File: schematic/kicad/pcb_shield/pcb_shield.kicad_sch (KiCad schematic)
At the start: 15 parts, among them J1 CN7, J2 CN10

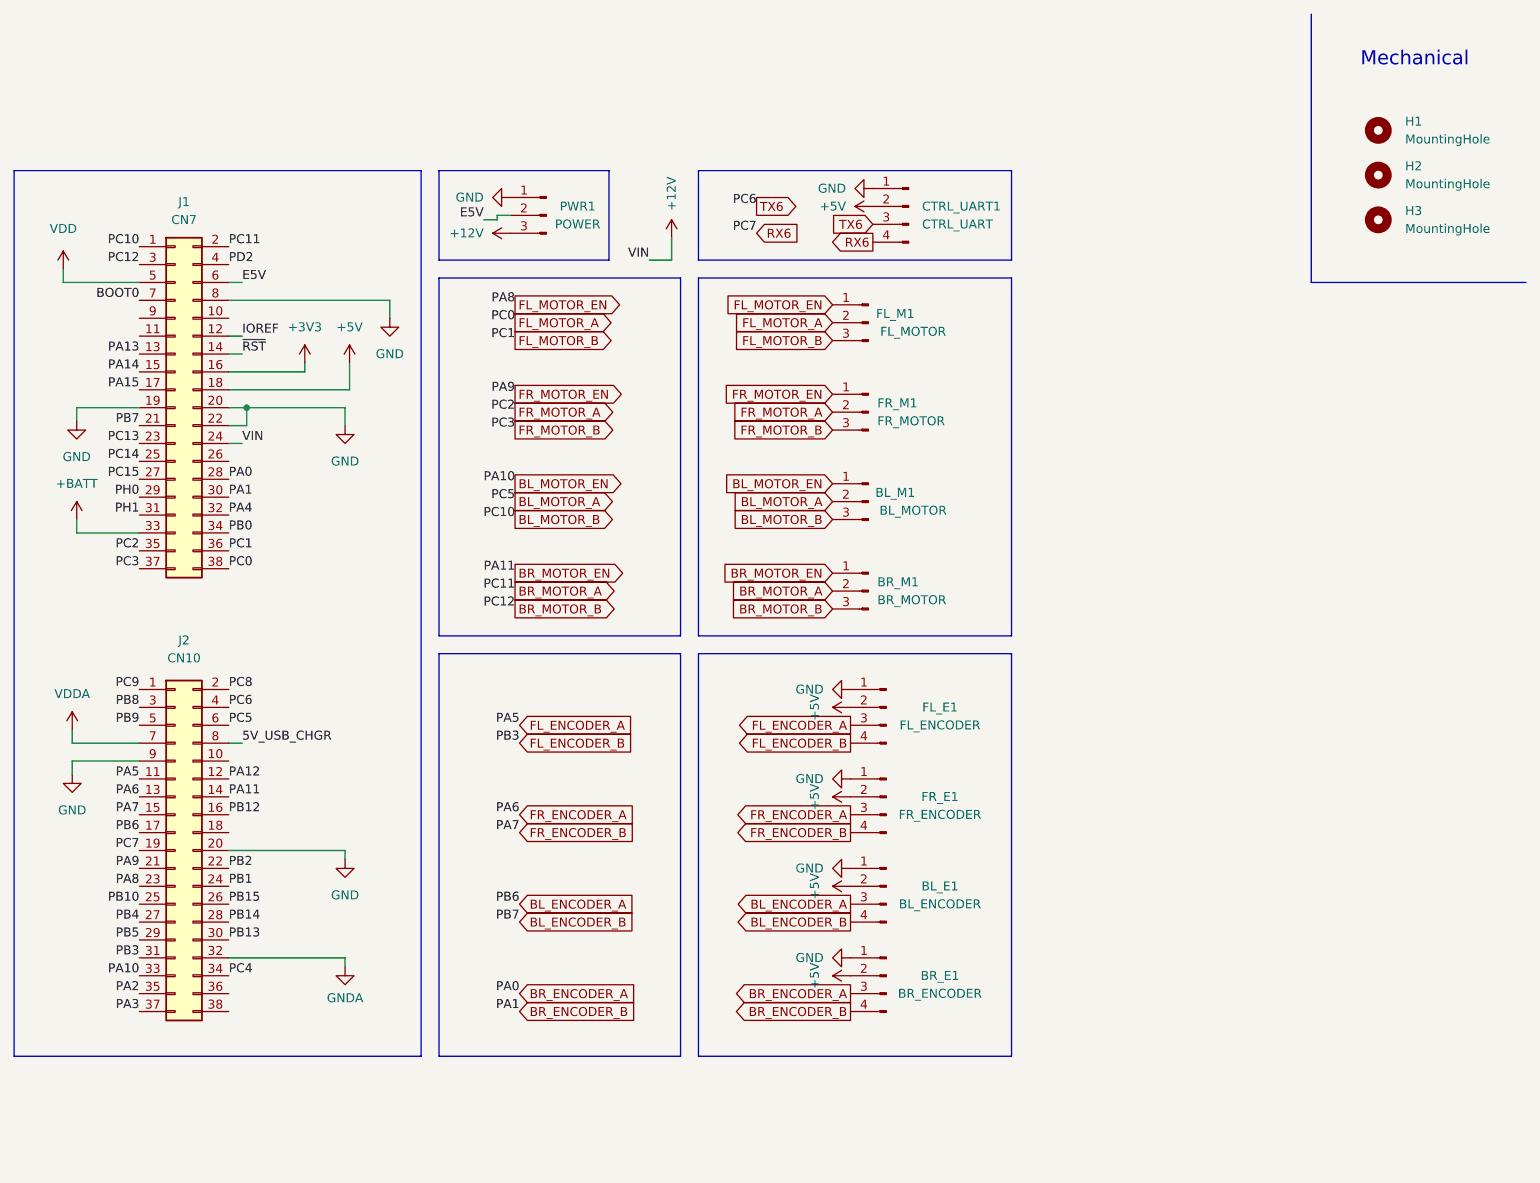
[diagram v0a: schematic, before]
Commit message: pcb maintenance: no connect, updated erc, fix a few erc warnings/errors
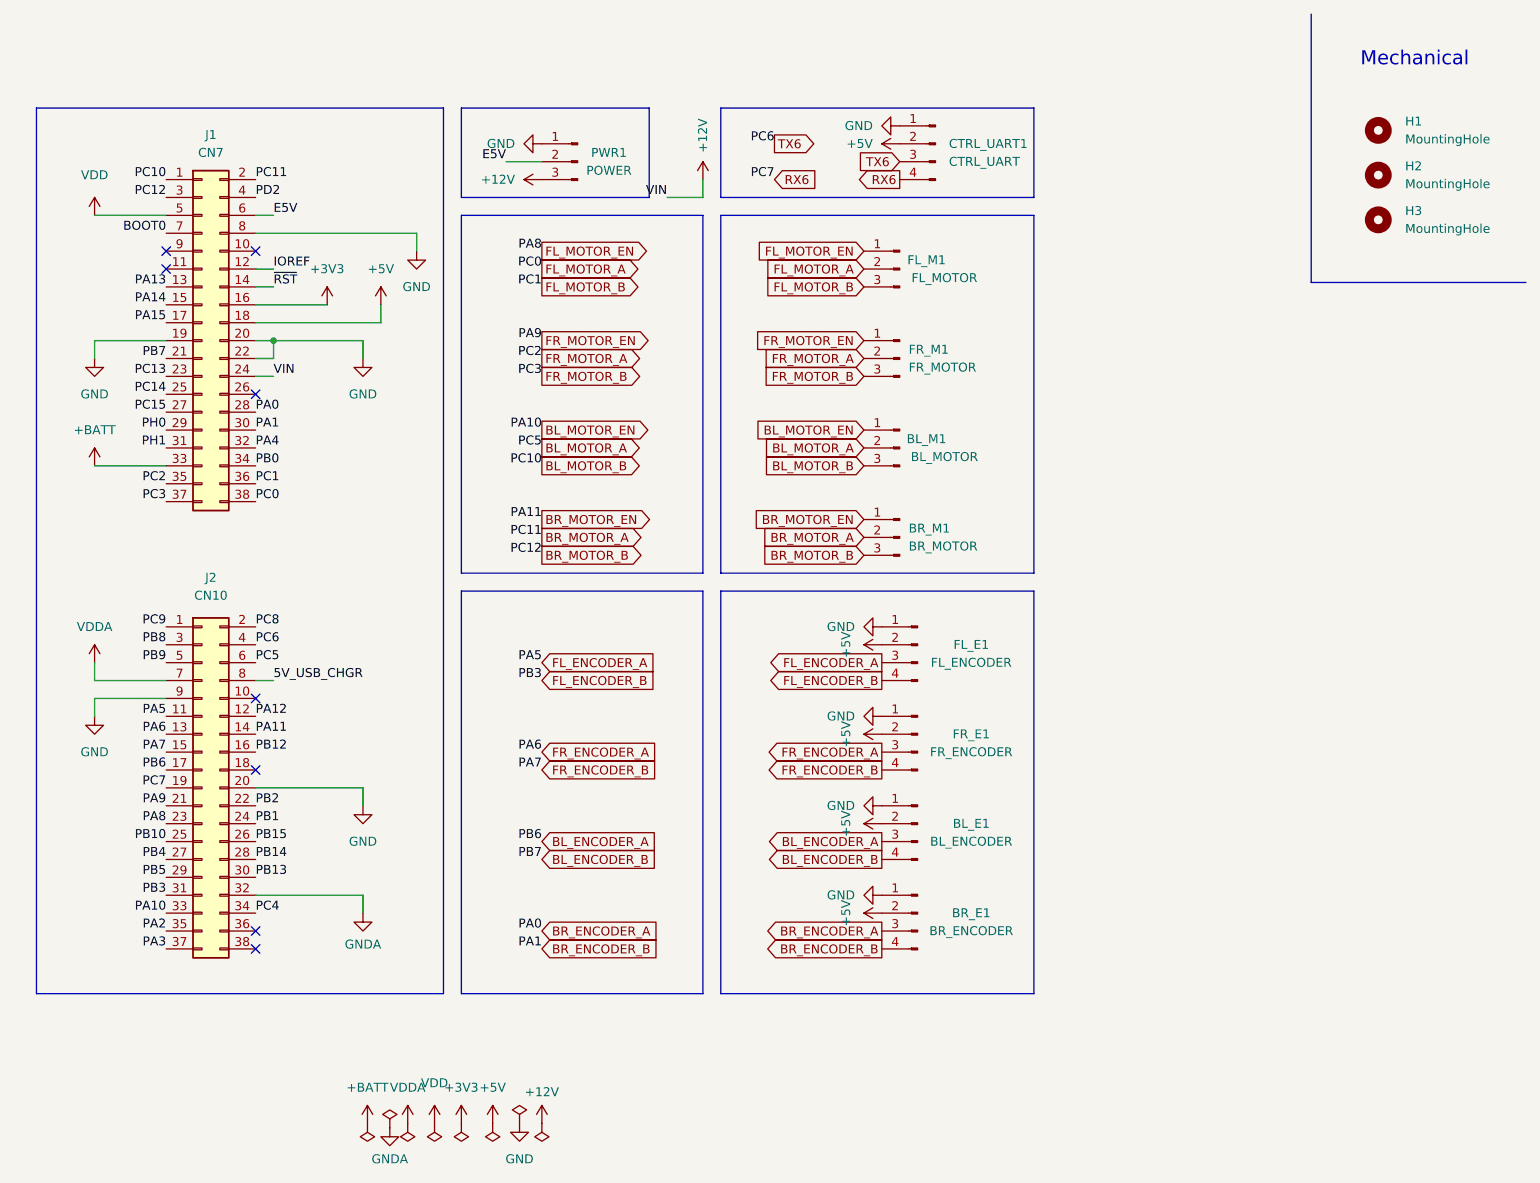
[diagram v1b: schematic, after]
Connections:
- no-connect marks 0 -> 8
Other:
- moved on the sheet: BL_E1, BL_M1, BR_E1, BR_M1, CTRL_UART1, FL_E1, FL_M1, FR_E1, FR_M1, J1, J2, PWR1
